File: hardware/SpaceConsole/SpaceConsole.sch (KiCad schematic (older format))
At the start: 11 parts, among them IC1 ArduinoProMini, J1 LeftFrontLED, J2 RightFrontLED, J3 LeftMiddleLED, J4 RightMiddleLED, J5 RearLED, J6 SwitchA, J7 Battery, J8 Conn_01x09_Male, J9 Power_Switch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

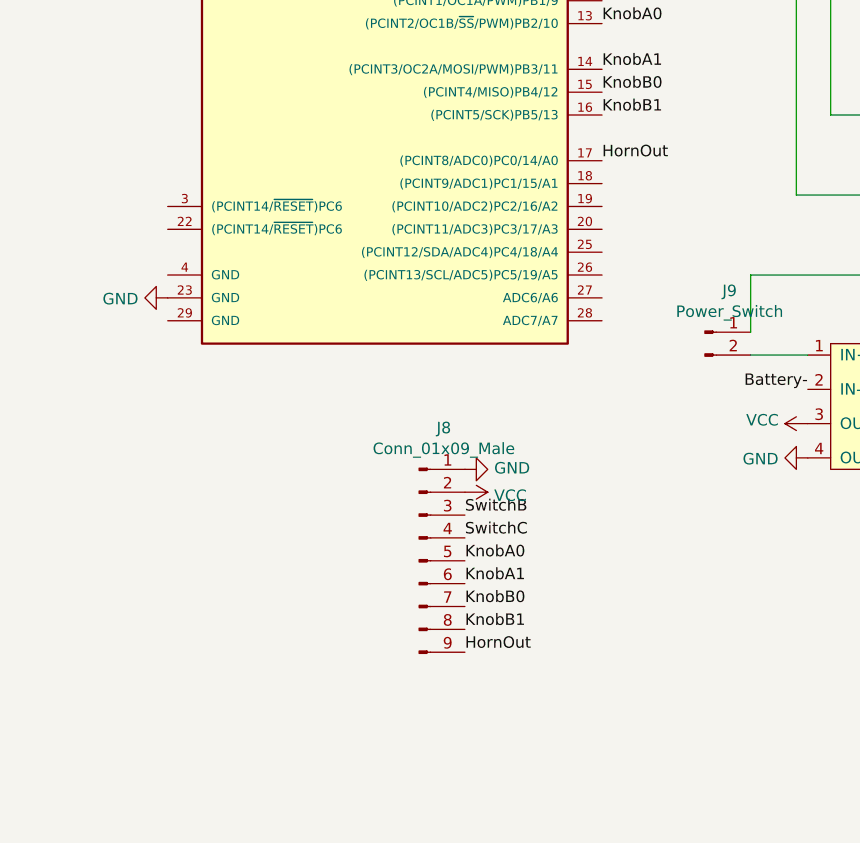
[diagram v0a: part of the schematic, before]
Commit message: Add knobs and switches to schematic
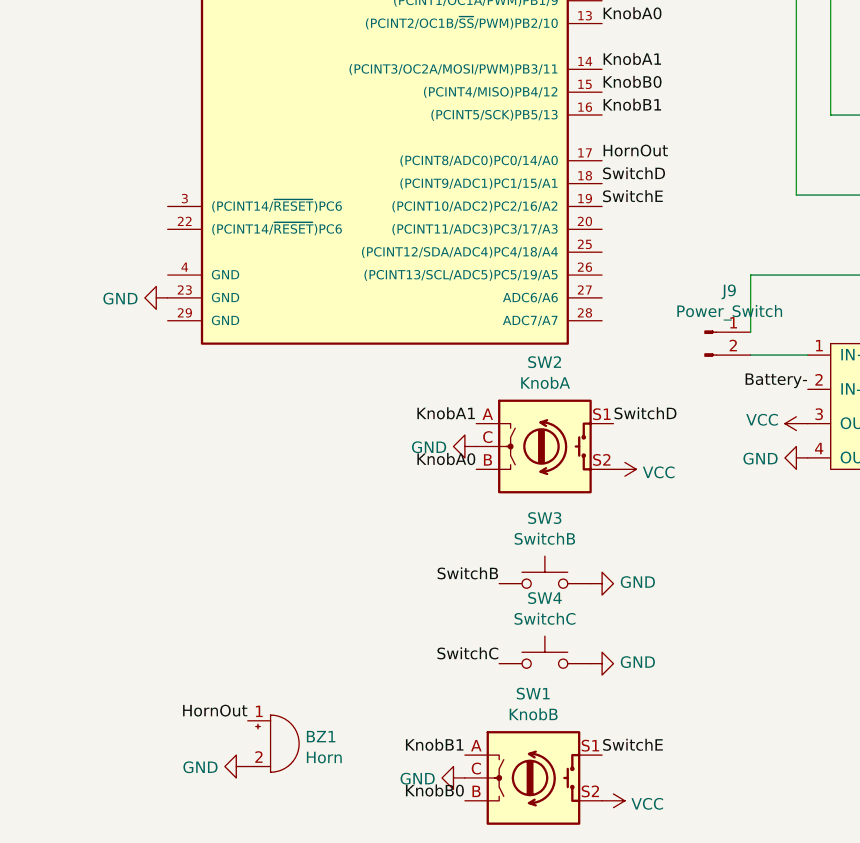
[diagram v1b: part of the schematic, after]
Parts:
- removed J8: Conn_01x09_Male, Connector_PinHeader_2.54mm:PinHeader_1x09_P2.54mm_Vertical, symbol Connector:Conn_01x09_Male
- added BZ1: Horn, symbol Device:Buzzer
- added SW1: KnobB, symbol Device:Rotary_Encoder_Switch
- added SW2: KnobA, symbol Device:Rotary_Encoder_Switch
- added SW3: SwitchB, symbol Switch:SW_Push
- added SW4: SwitchC, symbol Switch:SW_Push
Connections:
- net GND: now also BZ1.2 (+), SW1.C, SW2.C, SW3.2, SW4.2
- net HornOut: now also BZ1.1 (-)
- net KnobA0: now also SW2.B
- net KnobA1: now also SW2.A
- net KnobB0: now also SW1.B
- net KnobB1: now also SW1.A
- net SwitchB: now also SW3.1
- net SwitchC: now also SW4.1
- net VCC: now also SW1.S2, SW2.S2
- net SwitchD: now reaches IC1.18 ((PCINT9/ADC1)PC1/15/A1)
- net SwitchD: now also SW2.S1
- net SwitchE: now reaches IC1.19 ((PCINT10/ADC2)PC2/16/A2)
- net SwitchE: now also SW1.S1
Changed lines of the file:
@@
 Battery-
-$Comp
-L Connector:Conn_01x09_Male J8
-U 1 1 5FBB2A1F
-P 5450 6400
-F 0 "J8" H 5558 6981 50  0000 C CNN
-F 1 "Conn_01x09_Male" H 5558 6890 50  0000 C CNN
-F 2 "Connector_PinHeader_2.54mm:PinHeader_1x09_P2.54mm_Vertical" H 5450 6400 50  0001 C CNN
-F 3 "~" H 5450 6400 50  0001 C CNN
-	1    5450 6400
-	1    0    0    -1
-$EndComp
-$Comp
-L power:GND #PWR04
-U 1 1 5FBB4227
-P 5650 6000
-F 0 "#PWR04" H 5650 5750 50  0001 C CNN
-F 1 "GND" V 5655 5872 50  0000 R CNN
-F 2 "" H 5650 6000 50  0001 C CNN
-F 3 "" H 5650 6000 50  0001 C CNN
-	1    5650 6000
-	0    -1   -1   0
-$EndComp
-$Comp
-L power:VCC #PWR05
-U 1 1 5FBB4E89
-P 5650 6100
-F 0 "#PWR05" H 5650 5950 50  0001 C CNN
-F 1 "VCC" V 5665 6228 50  0000 L CNN
-F 2 "" H 5650 6100 50  0001 C CNN
-F 3 "" H 5650 6100 50  0001 C CNN
-	1    5650 6100
-	0    1    1    0
-$EndComp
-Text Label 5650 6200 0    50   ~ 0
-SwitchB
-Text Label 5650 6300 0    50   ~ 0
-SwitchC
-Text Label 5650 6400 0    50   ~ 0
-KnobA0
-Text Label 5650 6500 0    50   ~ 0
-KnobA1
-Text Label 5650 6600 0    50   ~ 0
-KnobB0
-Text Label 5650 6700 0    50   ~ 0
-KnobB1
-Text Label 5650 6800 0    50   ~ 0
-HornOut
 $Comp
 L Connector:Screw_Terminal_01x02 J7
@@
 Wire Wire Line
 	6900 5500 7150 5500
+$Comp
+L Device:Rotary_Encoder_Switch SW2
+U 1 1 5FC31CA7
+P 6000 5900
+F 0 "SW2" H 6000 6267 50  0000 C CNN
+F 1 "KnobA" H 6000 6176 50  0000 C CNN
+F 2 "" H 5850 6060 50  0001 C CNN
+F 3 "~" H 6000 6160 50  0001 C CNN
+	1    6000 5900
+	1    0    0    -1
+$EndComp
+$Comp
+L Device:Rotary_Encoder_Switch SW1
+U 1 1 5FC32224
+P 5950 7350
+F 0 "SW1" H 5950 7717 50  0000 C CNN
+F 1 "KnobB" H 5950 7626 50  0000 C CNN
+F 2 "" H 5800 7510 50  0001 C CNN
+F 3 "~" H 5950 7610 50  0001 C CNN
+	1    5950 7350
+	1    0    0    -1
+$EndComp
+$Comp
+L Switch:SW_Push SW3
+U 1 1 5FC3BF74
+P 6000 6500
+F 0 "SW3" H 6000 6785 50  0000 C CNN
+F 1 "SwitchB" H 6000 6694 50  0000 C CNN
+F 2 "" H 6000 6700 50  0001 C CNN
+F 3 "~" H 6000 6700 50  0001 C CNN
+	1    6000 6500
+	1    0    0    -1
+$EndComp
+$Comp
+L Switch:SW_Push SW4
+U 1 1 5FC3C79A
+P 6000 6850
+F 0 "SW4" H 6000 7135 50  0000 C CNN
+F 1 "SwitchC" H 6000 7044 50  0000 C CNN
+F 2 "" H 6000 7050 50  0001 C CNN
+F 3 "~" H 6000 7050 50  0001 C CNN
+	1    6000 6850
+	1    0    0    -1
+$EndComp
+$Comp
+L Device:Buzzer BZ1
+U 1 1 5FC3E295
+P 4800 7200
+F 0 "BZ1" H 4952 7229 50  0000 L CNN
+F 1 "Horn" H 4952 7138 50  0000 L CNN
+F 2 "" V 4775 7300 50  0001 C CNN
+F 3 "~" V 4775 7300 50  0001 C CNN
+	1    4800 7200
+	1    0    0    -1
+$EndComp
+$Comp
+L power:GND #PWR02
+U 1 1 5FC3F88F
+P 4700 7300
+F 0 "#PWR02" H 4700 7050 50  0001 C CNN
+F 1 "GND" V 4705 7172 50  0000 R CNN
+F 2 "" H 4700 7300 50  0001 C CNN
+F 3 "" H 4700 7300 50  0001 C CNN
+	1    4700 7300
+	0    1    1    0
+$EndComp
+$Comp
+L power:GND #PWR018
+U 1 1 5FC40A22
+P 5650 7350
+F 0 "#PWR018" H 5650 7100 50  0001 C CNN
+F 1 "GND" V 5655 7222 50  0000 R CNN
+F 2 "" H 5650 7350 50  0001 C CNN
+F 3 "" H 5650 7350 50  0001 C CNN
+	1    5650 7350
+	0    1    1    0
+$EndComp
+$Comp
+L power:GND #PWR019
+U 1 1 5FC4124B
+P 5700 5900
+F 0 "#PWR019" H 5700 5650 50  0001 C CNN
+F 1 "GND" V 5705 5772 50  0000 R CNN
+F 2 "" H 5700 5900 50  0001 C CNN
+F 3 "" H 5700 5900 50  0001 C CNN
+	1    5700 5900
+	0    1    1    0
+$EndComp
+Text Label 5800 6500 2    50   ~ 0
+SwitchB
+$Comp
+L power:GND #PWR020
+U 1 1 5FC43290
+P 6200 6500
+F 0 "#PWR020" H 6200 6250 50  0001 C CNN
+F 1 "GND" V 6205 6372 50  0000 R CNN
+F 2 "" H 6200 6500 50  0001 C CNN
+F 3 "" H 6200 6500 50  0001 C CNN
+	1    6200 6500
+	0    -1   -1   0
+$EndComp
+$Comp
+L power:GND #PWR021
+U 1 1 5FC437ED
+P 6200 6850
+F 0 "#PWR021" H 6200 6600 50  0001 C CNN
+F 1 "GND" V 6205 6722 50  0000 R CNN
+F 2 "" H 6200 6850 50  0001 C CNN
+F 3 "" H 6200 6850 50  0001 C CNN
+	1    6200 6850
+	0    -1   -1   0
+$EndComp
+Text Label 5800 6850 2    50   ~ 0
+SwitchC
+Text Label 5650 7250 2    50   ~ 0
+KnobB1
+Text Label 5650 7450 2    50   ~ 0
+KnobB0
+Text Label 5700 5800 2    50   ~ 0
+KnobA1
+Text Label 5700 6000 2    50   ~ 0
+KnobA0
+$Comp
+L power:VCC #PWR023
+U 1 1 5FC47472
+P 6300 6000
+F 0 "#PWR023" H 6300 5850 50  0001 C CNN
+F 1 "VCC" V 6315 6128 50  0000 L CNN
+F 2 "" H 6300 6000 50  0001 C CNN
+F 3 "" H 6300 6000 50  0001 C CNN
+	1    6300 6000
+	0    1    1    0
+$EndComp
+$Comp
+L power:VCC #PWR022
+U 1 1 5FC479DD
+P 6250 7450
+F 0 "#PWR022" H 6250 7300 50  0001 C CNN
+F 1 "VCC" V 6265 7578 50  0000 L CNN
+F 2 "" H 6250 7450 50  0001 C CNN
+F 3 "" H 6250 7450 50  0001 C CNN
+	1    6250 7450
+	0    1    1    0
+$EndComp
+Text Label 6250 4750 0    50   ~ 0
+SwitchD
+Text Label 6250 4850 0    50   ~ 0
+SwitchE
+Text Label 6300 5800 0    50   ~ 0
+SwitchD
+Text Label 6250 7250 0    50   ~ 0
+SwitchE
+Text Label 4700 7100 2    50   ~ 0
+HornOut
 $EndSCHEMATC

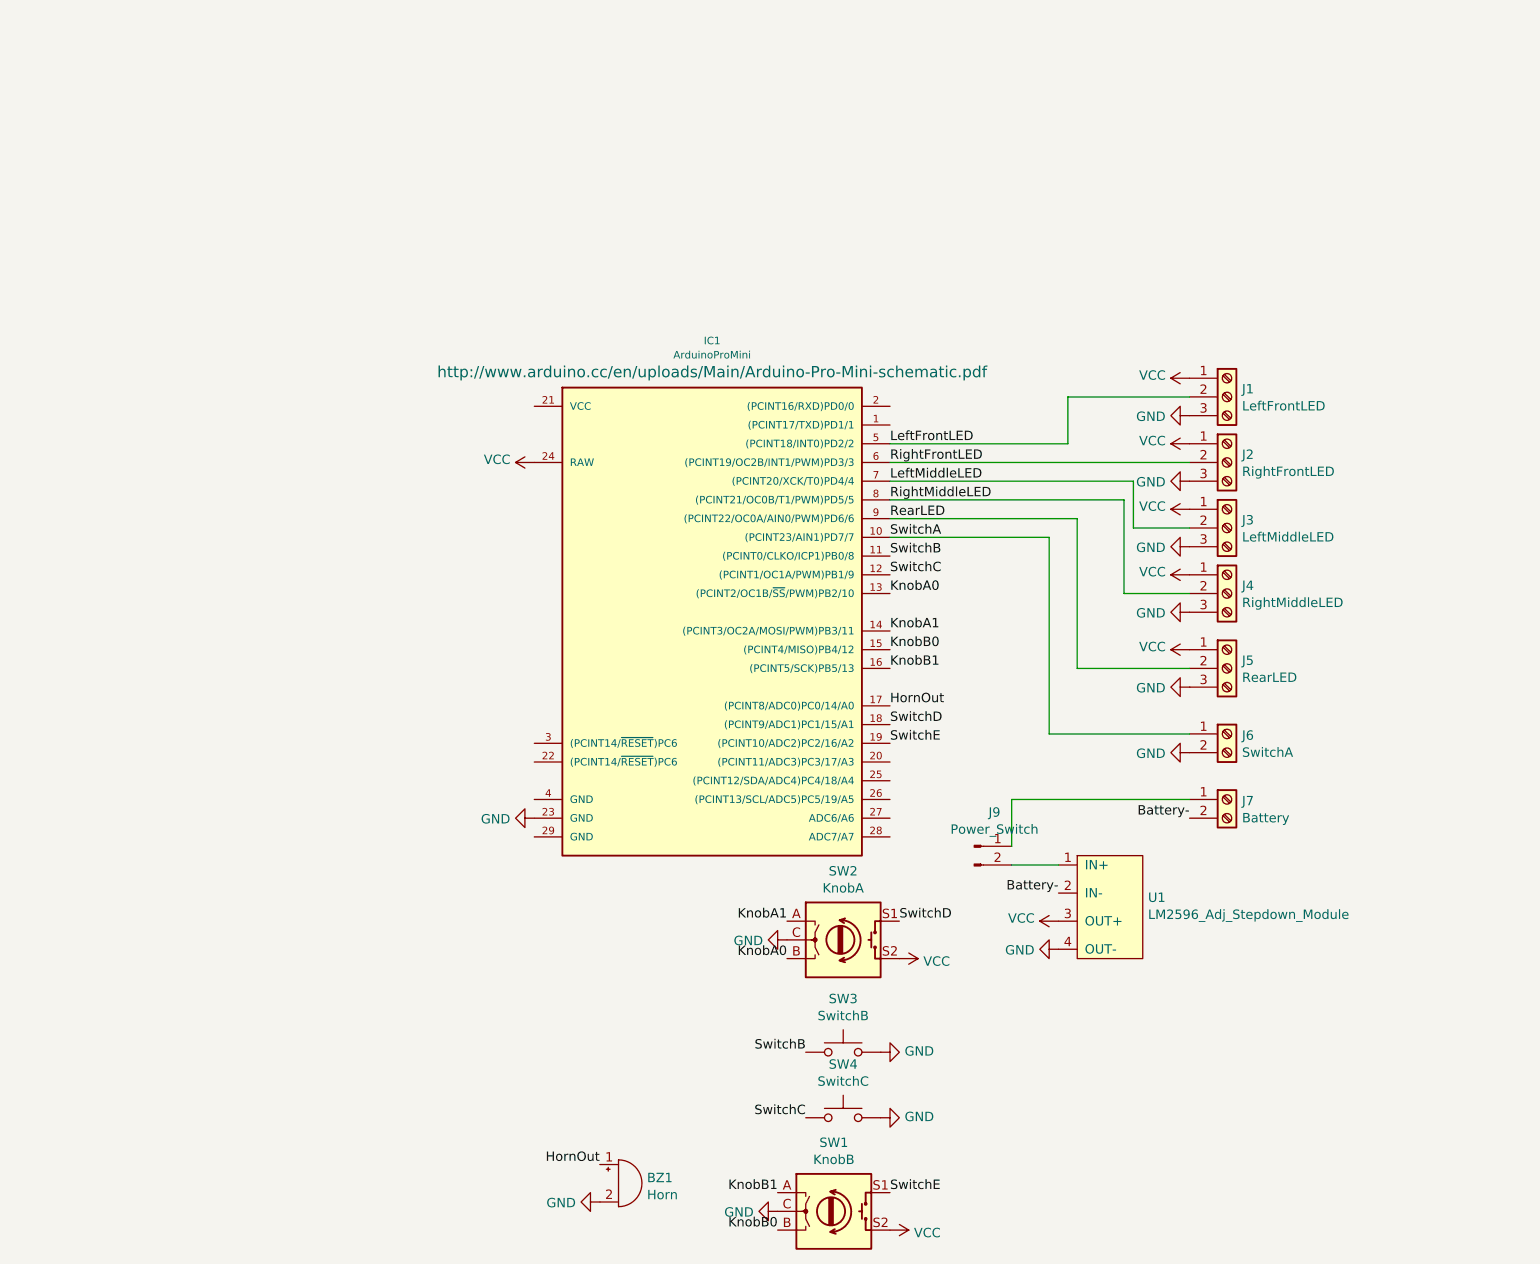
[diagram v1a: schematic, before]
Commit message: Add routing for knobs and switches
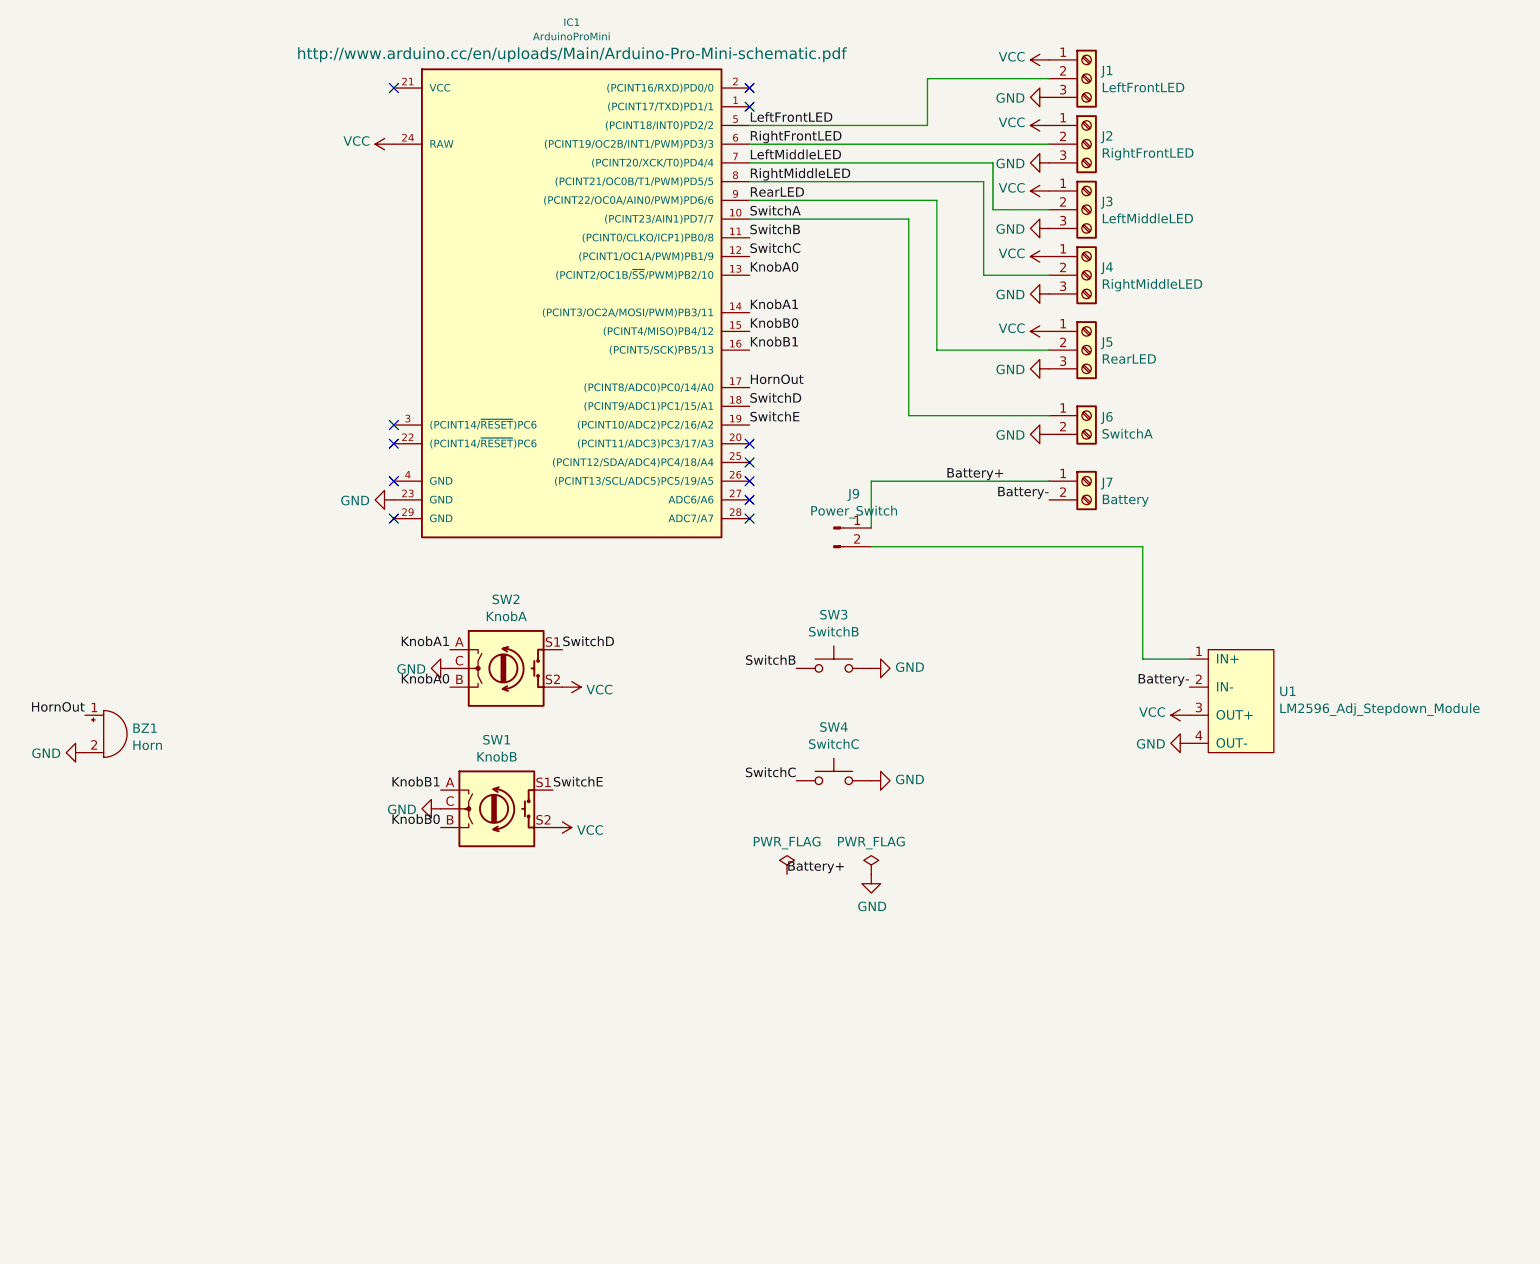
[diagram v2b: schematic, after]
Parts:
- BZ1: footprint (none) -> Buzzer_Beeper:Buzzer_TDK_PS1240P02BT_D12.2mm_H6.5mm
- SW1, SW2: footprint (none) -> Connector_PinHeader_2.54mm:PinHeader_1x05_P2.54mm_Vertical
- SW3, SW4: footprint (none) -> Connector_PinHeader_2.54mm:PinHeader_1x02_P2.54mm_Vertical
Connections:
- net Battery+: now reaches J7.1 (Pin_1), J9.1 (Pin_1)
- no-connect marks 0 -> 12
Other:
- moved on the sheet: BZ1, IC1, J1, J2, J3, J4, J5, J6, J7, J9, SW1, SW2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

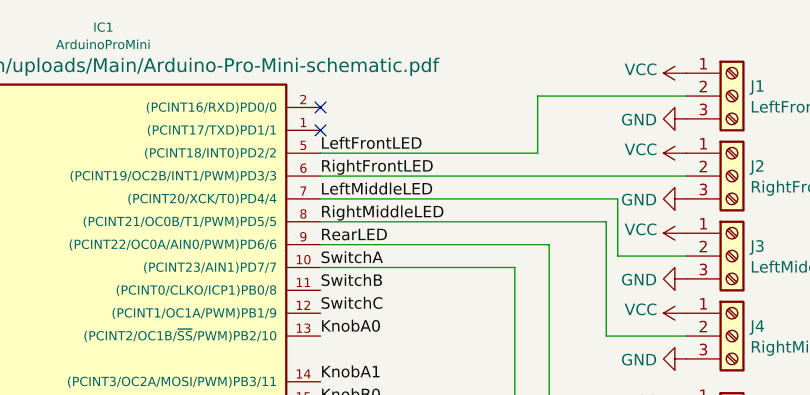
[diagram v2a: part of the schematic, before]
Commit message: Update silk screen
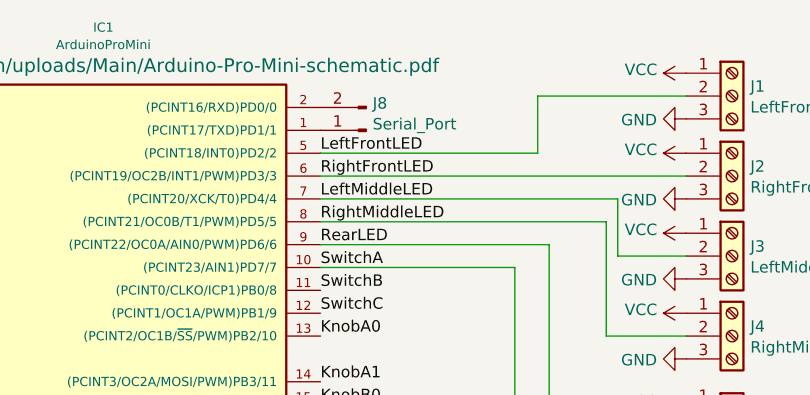
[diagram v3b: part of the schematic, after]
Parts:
- added J8: Serial_Port, Connector_PinHeader_2.54mm:PinHeader_1x02_P2.54mm_Vertical, symbol Connector:Conn_01x02_Male
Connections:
- net at IC1.1 ((PCINT17/TXD)PD1/1): now also J8.1 (Pin_1)
- net at IC1.2 ((PCINT16/RXD)PD0/0): now also J8.2 (Pin_2)
- no-connect marks 12 -> 10
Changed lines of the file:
@@
 $EndDescr
-$Comp
-L mysensors_arduino:ArduinoProMini IC1
-U 1 1 5FB7EAFA
-P 4500 2450
-F 0 "IC1" H 4550 3900 40  0000 C CNN
-F 1 "ArduinoProMini" H 4550 3824 40  0000 C CNN
-F 2 "mysensors_arduino:pro_mini" H 4500 2450 30  0001 C CIN
-F 3 "http://www.arduino.cc/en/uploads/Main/Arduino-Pro-Mini-schematic.pdf" H 4550 3733 60  0000 C CNN
-	1    4500 2450
-	1    0    0    -1
-$EndComp
 $Comp
 L power:VCC #PWR01
@@
 NoConn ~ 3600 3150
 NoConn ~ 3600 1350
-NoConn ~ 5500 1350
-NoConn ~ 5500 1450
 NoConn ~ 5500 3250
 NoConn ~ 5500 3350
@@
 Text Label 5700 5550 0    50   ~ 0
 Battery+
+$Comp
+L mysensors_arduino:ArduinoProMini IC1
+U 1 1 5FB7EAFA
+P 4500 2450
+F 0 "IC1" H 4550 3900 40  0000 C CNN
+F 1 "ArduinoProMini" H 4550 3824 40  0000 C CNN
+F 2 "mysensors_arduino:pro_mini" H 4500 2450 30  0001 C CIN
+F 3 "http://www.arduino.cc/en/uploads/Main/Arduino-Pro-Mini-schematic.pdf" H 4550 3733 60  0000 C CNN
+	1    4500 2450
+	1    0    0    -1
+$EndComp
+$Comp
+L Connector:Conn_01x02_Male J8
+U 1 1 5FCB646F
+P 5700 1450
+F 0 "J8" H 5672 1332 50  0000 R CNN
+F 1 "Serial_Port" H 5672 1423 50  0000 R CNN
+F 2 "Connector_PinHeader_2.54mm:PinHeader_1x02_P2.54mm_Vertical" H 5700 1450 50  0001 C CNN
+F 3 "~" H 5700 1450 50  0001 C CNN
+	1    5700 1450
+	-1   0    0    1
+$EndComp
 $EndSCHEMATC
